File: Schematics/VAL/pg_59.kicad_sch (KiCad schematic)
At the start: 12 parts, among them U6101 F260, U6102 F10, U6103 F260, U6104 F10, U6105 F74, U6106 F74, U6107 F74, U6108 F74, U6109 F37, U6110 F260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

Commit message: Use backplane clocks
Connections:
- net UIR~.SCLK.B2 renamed UIR~.SCLK
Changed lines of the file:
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@@
   (wire (pts (xy 368.3 55.88) (xy 375.92 55.88) ) )
   (wire (pts (xy 368.3 93.98) (xy 375.92 93.98) ) )
-  (global_label "UIR~.SCLK.B2" (shape input) (at 111.76 27.94 180) (fields_autoplaced) (effects (font (size 2.54 2.54) ) (justify right) ) (property "Intersheet References" "${INTERSHEET_REFS}" (id 0) (at 81.7759 27.7813 0) (effects (font (size 2.54 2.54) ) (justify right) ) ) )
+  (global_label "UIR~.SCLK" (shape input) (at 111.76 27.94 180) (fields_autoplaced) (effects (font (size 2.54 2.54) ) (justify right) ) (property "Intersheet References" "${INTERSHEET_REFS}" (id 0) (at 81.7759 27.7813 0) (effects (font (size 2.54 2.54) ) (justify right) ) ) )
   (global_label "WCS.D[0..11]" (shape input) (at 112.6531 38.1 180) (fields_autoplaced) (effects (font (size 2.54 2.54) ) (justify right) ) (property "Intersheet References" "${INTERSHEET_REFS}" (id 0) (at 83.1528 37.9413 0) (effects (font (size 2.54 2.54) ) (justify right) ) ) )
   (bus_entry (at 116.84 40.64) (size 2.54 2.54) )

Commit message: Speed up VAL board
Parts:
- removed U6101, U6103, U6110, U6112: F260, symbol r1000:F260
- removed U6102, U6104: F10, symbol r1000:F10
- removed U6105, U6106, U6107, U6108: F74, symbol r1000:F74
- removed U6109, U6111: F37, symbol r1000:F37
- added U6113, U6115: F521, symbol r1000:F521
- added U6114, U6116: F74, symbol r1000:F74
- added U6117, U6118: F02, symbol r1000:F02
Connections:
- net A_LOOP_DEC: now also U6117.3 (Q)
- net A_LOOP_DEC~: now also U6114.5 (Q), U6117.1 (D0)
- net B_LOOP_DEC: now also U6118.3 (Q)
- net B_LOOP_DEC~: now also U6116.5 (Q), U6118.1 (D0)
- net H2: now also U6117.2 (D1), U6118.2 (D1)
- net PD: now also U6113.1 (E), U6113.12 (B4), U6113.14 (B5), U6113.7 (B2), U6115.1 (E), U6115.12 (B4), U6115.14 (B5), U6115.7 (B2)
- net PU: now also U6113.16 (B6), U6113.18 (B7), U6113.9 (B3), U6114.1 (CL_), U6114.4 (PR_), U6115.16 (B6), U6115.18 (B7), U6115.9 (B3), U6116.1 (CL_), U6116.4 (PR_)
- net UIR~.SCLK: now also U6114.3 (CLK), U6116.3 (CLK)
- net WCS.D0: now also U6113.6 (A2)
- net WCS.D1: now also U6113.8 (A3)
- net WCS.D10: now also U6115.15 (A6)
- net WCS.D11: now also U6115.17 (A7)
- net WCS.D2: now also U6113.11 (A4)
- net WCS.D3: now also U6113.13 (A5)
- net WCS.D4: now also U6113.15 (A6)
- net WCS.D5: now also U6113.17 (A7)
- net WCS.D6: now also U6115.6 (A2)
- net WCS.D7: now also U6115.8 (A3)
- net WCS.D8: now also U6115.11 (A4)
- net WCS.D9: now also U6115.13 (A5)
- new net: U6113.19 (A=B), U6114.2 (D)
- new net: U6115.19 (A=B), U6116.2 (D)
- no-connect marks 0 -> 10
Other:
- note added: "UIR.A0"
- note added: "UIR.A1"
- note added: "UIR.A2"
- note added: "UIR.A3"
- note added: "UIR.A4"
- note added: "UIR.A5"
- note added: "UIR.B0"
- note added: "UIR.B1"
- note added: "UIR.B2"
- note added: "UIR.B3"
- note added: "UIR.B4"
- note added: "UIR.B5"

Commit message: KiCad 6
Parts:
- U6113, U6115: value F521 -> (none)
- U6114, U6116: value F74 -> (none)
- U6117, U6118: value F02 -> (none)

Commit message: Recover from KiCad-6 munging
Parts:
- U6113, U6115: value (none) -> F521
- U6114, U6116: value (none) -> F74
- U6117, U6118: value (none) -> F02

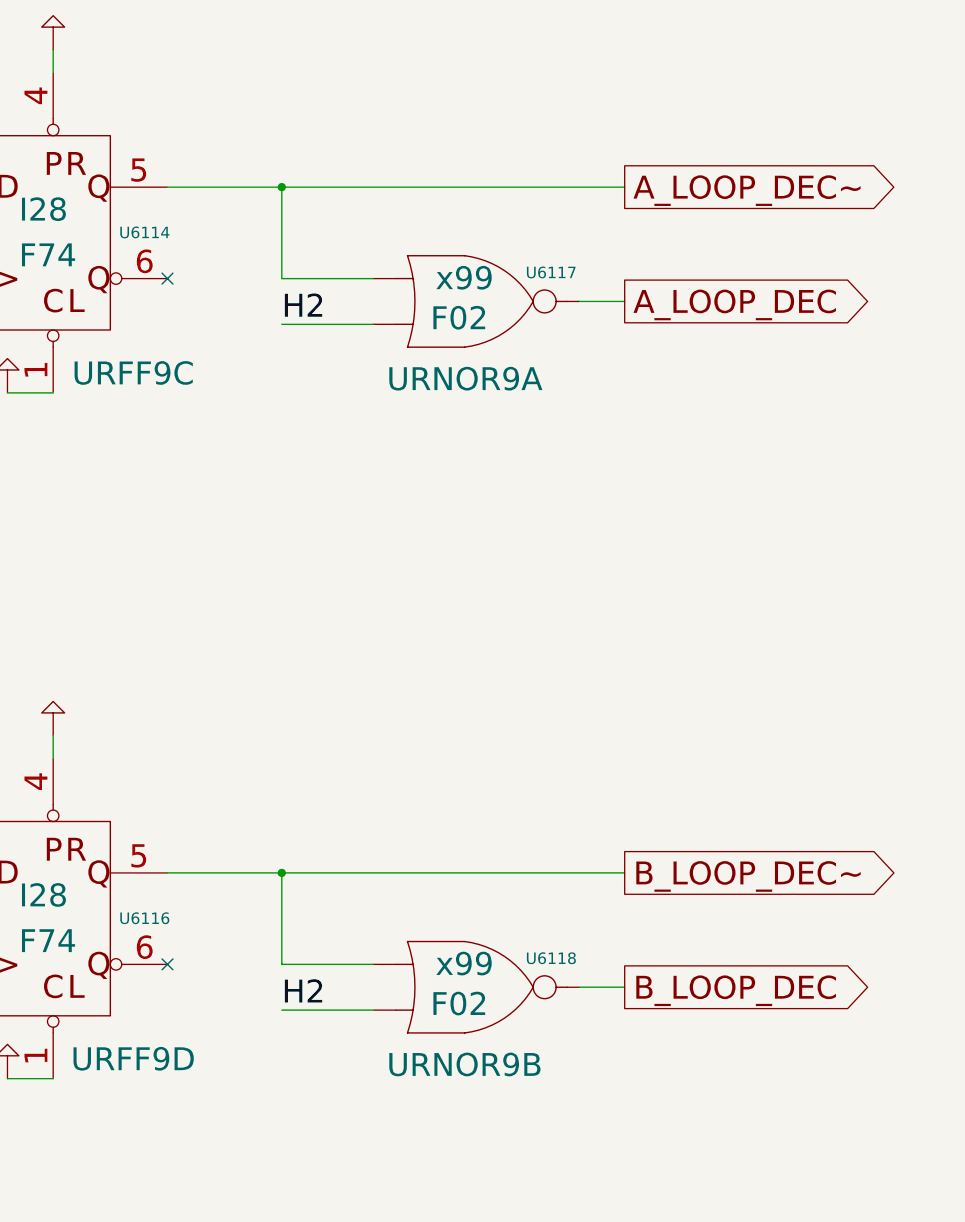
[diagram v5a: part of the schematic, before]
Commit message: Snapshot with some significant speedups.
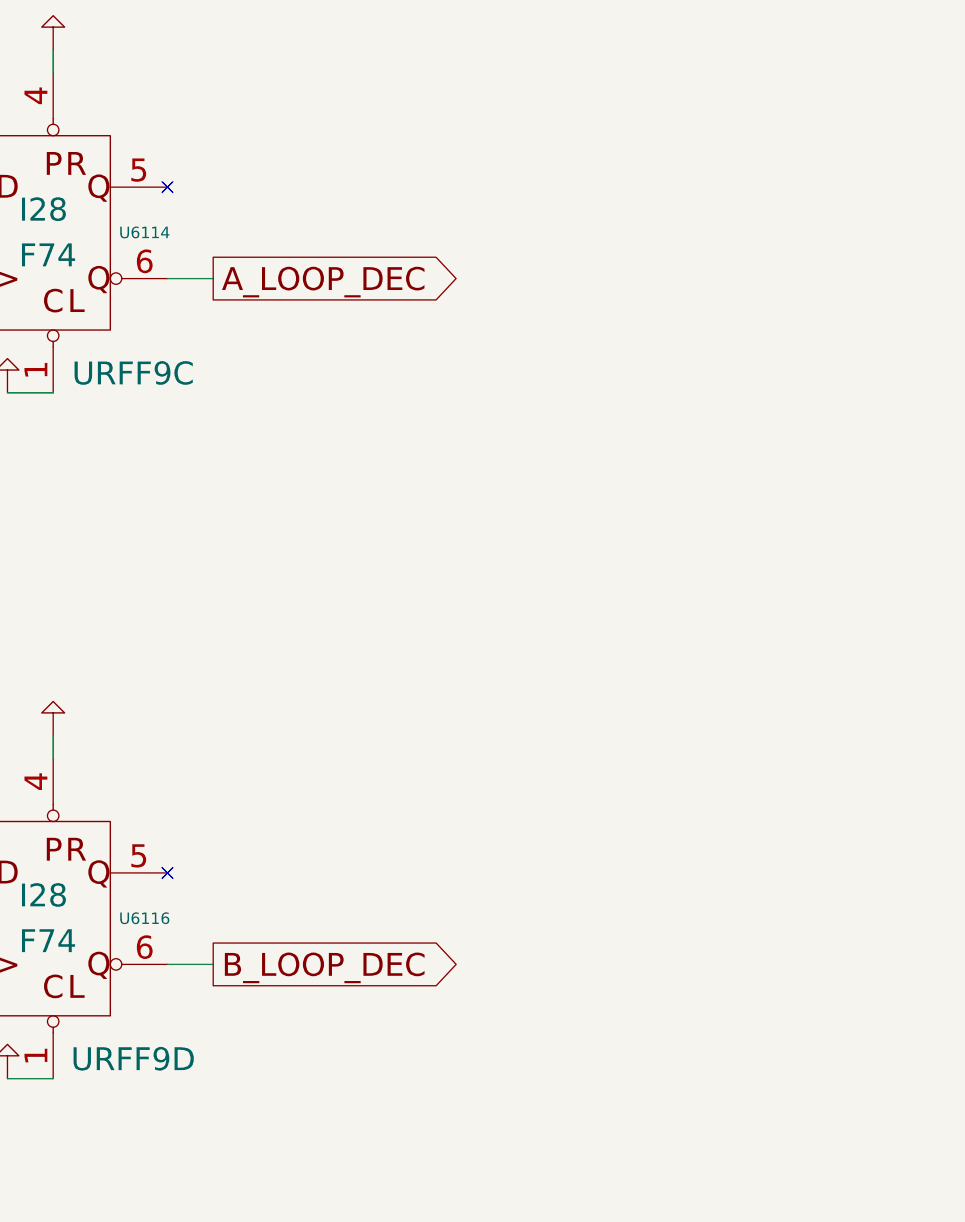
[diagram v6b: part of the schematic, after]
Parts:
- removed U6117, U6118: F02, symbol r1000:F02
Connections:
- net A_LOOP_DEC: now also U6114.6 (Q_)
- net B_LOOP_DEC: now also U6116.6 (Q_)
- net A_LOOP_DEC~: no longer names the net of U6114.5 (Q)
- net B_LOOP_DEC~: no longer names the net of U6116.5 (Q)
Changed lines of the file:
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@@
   (wire (pts (xy 289.56 109.22) (xy 289.56 111.76) ) )
   (wire (pts (xy 289.56 185.42) (xy 289.56 187.96) ) )
-  (wire (pts (xy 302.26 124.46) (xy 314.96 124.46) ) )
-  (wire (pts (xy 302.26 200.66) (xy 314.96 200.66) ) )
-  (wire (pts (xy 314.96 124.46) (xy 353.06 124.46) ) )
-  (wire (pts (xy 314.96 134.62) (xy 314.96 124.46) ) )
-  (wire (pts (xy 314.96 139.7) (xy 325.12 139.7) ) )
-  (wire (pts (xy 314.96 200.66) (xy 353.06 200.66) ) )
-  (wire (pts (xy 314.96 210.82) (xy 314.96 200.66) ) )
-  (wire (pts (xy 314.96 215.9) (xy 325.12 215.9) ) )
-  (wire (pts (xy 325.12 134.62) (xy 314.96 134.62) ) )
-  (wire (pts (xy 325.12 210.82) (xy 314.96 210.82) ) )
-  (wire (pts (xy 347.98 137.16) (xy 353.06 137.16) ) )
-  (wire (pts (xy 347.98 213.36) (xy 353.06 213.36) ) )
+  (wire (pts (xy 302.26 134.62) (xy 307.34 134.62) ) )
+  (wire (pts (xy 302.26 210.82) (xy 307.34 210.82) ) )
   (wire (pts (xy 76.2 12.7) (xy 88.9 12.7) ) )
   (wire (pts (xy 76.2 22.86) (xy 88.9 22.86) ) )
@@
   (symbol (lib_id "r1000:PU") (at 289.56 109.22 0) (unit 1) (in_bom yes) (on_board yes) (property "Reference" "#PWR06117" (id 0) (at 289.56 109.22 0) (effects (font (size 1.27 1.27) ) hide ) ) (property "Value" "PU" (id 1) (at 289.56 109.22 0) (effects (font (size 1.27 1.27) ) hide ) ) (property "Footprint" "" (id 2) (at 289.56 109.22 0) (effects (font (size 1.27 1.27) ) hide ) ) (property "Datasheet" "" (id 3) (at 289.56 109.22 0) (effects (font (size 1.27 1.27) ) hide ) ) (pin "1") )
   (symbol (lib_id "r1000:PU") (at 289.56 185.42 0) (unit 1) (in_bom yes) (on_board yes) (property "Reference" "#PWR06122" (id 0) (at 289.56 185.42 0) (effects (font (size 1.27 1.27) ) hide ) ) (property "Value" "PU" (id 1) (at 289.56 185.42 0) (effects (font (size 1.27 1.27) ) hide ) ) (property "Footprint" "" (id 2) (at 289.56 185.42 0) (effects (font (size 1.27 1.27) ) hide ) ) (property "Datasheet" "" (id 3) (at 289.56 185.42 0) (effects (font (size 1.27 1.27) ) hide ) ) (pin "1") )
-  (no_connect (at 302.26 134.62) )
-  (no_connect (at 302.26 210.82) )
-  (junction (at 314.96 124.46) (diameter 0) (color 0 0 0 0) )
-  (label "H2" (at 314.96 139.7 0) (effects (font (size 2.54 2.54) ) (justify left bottom) ) )
-  (junction (at 314.96 200.66) (diameter 0) (color 0 0 0 0) )
-  (label "H2" (at 314.96 215.9 0) (effects (font (size 2.54 2.54) ) (justify left bottom) ) )
-  (symbol (lib_id "r1000:F02") (at 332.74 134.62 0) (unit 1) (in_bom yes) (on_board yes) (property "Reference" "U6117" (id 0) (at 344.9 133.985 0) (effects (font (size 1.27 1.27) ) ) ) (property "Value" "F02" (id 1) (at 331.47 139.065 0) (effects (font (size 2.54 2.54) ) (justify left) ) ) (property "Footprint" "" (id 2) (at 332.74 134.62 0) (effects (font (size 1.27 1.27) ) hide ) ) (property "Datasheet" "" (id 3) (at 332.74 134.62 0) (effects (font (size 1.27 1.27) ) hide ) ) (property "Location" "x99" (id 4) (at 335.28 134.62 0) (effects (font (size 2.54 2.54) ) ) ) (property "Name" "URNOR9A" (id 5) (at 335.28 147.32 0) (effects (font (size 2.54 2.54) ) (justify bottom) ) ) (pin "1") (pin "2") (pin "3") )
-  (symbol (lib_id "r1000:F02") (at 332.74 210.82 0) (unit 1) (in_bom yes) (on_board yes) (property "Reference" "U6118" (id 0) (at 344.9 210.185 0) (effects (font (size 1.27 1.27) ) ) ) (property "Value" "F02" (id 1) (at 331.47 215.265 0) (effects (font (size 2.54 2.54) ) (justify left) ) ) (property "Footprint" "" (id 2) (at 332.74 210.82 0) (effects (font (size 1.27 1.27) ) hide ) ) (property "Datasheet" "" (id 3) (at 332.74 210.82 0) (effects (font (size 1.27 1.27) ) hide ) ) (property "Location" "x99" (id 4) (at 335.28 210.82 0) (effects (font (size 2.54 2.54) ) ) ) (property "Name" "URNOR9B" (id 5) (at 335.28 223.52 0) (effects (font (size 2.54 2.54) ) (justify bottom) ) ) (pin "1") (pin "2") (pin "3") )
-  (global_label "A_LOOP_DEC~" (shape output) (at 353.06 124.46 0) (fields_autoplaced) (effects (font (size 2.54 2.54) ) (justify left) ) (property "Intersheet References" "${INTERSHEET_REFS}" (id 0) (at 383.0441 124.3013 0) (effects (font (size 1.905 1.905) ) (justify left) ) ) )
-  (global_label "A_LOOP_DEC" (shape output) (at 353.06 137.16 0) (fields_autoplaced) (effects (font (size 2.54 2.54) ) (justify left) ) (property "Intersheet References" "${INTERSHEET_REFS}" (id 0) (at 381.2298 137.0013 0) (effects (font (size 1.905 1.905) ) (justify left) ) ) )
-  (global_label "B_LOOP_DEC~" (shape output) (at 353.06 200.66 0) (fields_autoplaced) (effects (font (size 2.54 2.54) ) (justify left) ) (property "Intersheet References" "${INTERSHEET_REFS}" (id 0) (at 383.407 200.5013 0) (effects (font (size 1.905 1.905) ) (justify left) ) ) )
-  (global_label "B_LOOP_DEC" (shape output) (at 353.06 213.36 0) (fields_autoplaced) (effects (font (size 2.54 2.54) ) (justify left) ) (property "Intersheet References" "${INTERSHEET_REFS}" (id 0) (at 381.5927 213.2013 0) (effects (font (size 1.905 1.905) ) (justify left) ) ) )
+  (no_connect (at 302.26 124.46) )
+  (no_connect (at 302.26 200.66) )
+  (global_label "A_LOOP_DEC" (shape output) (at 307.34 134.62 0) (fields_autoplaced) (effects (font (size 2.54 2.54) ) (justify left) ) (property "Intersheet References" "${INTERSHEET_REFS}" (id 0) (at 335.5098 134.4613 0) (effects (font (size 1.905 1.905) ) (justify left) ) ) )
+  (global_label "B_LOOP_DEC" (shape output) (at 307.34 210.82 0) (fields_autoplaced) (effects (font (size 2.54 2.54) ) (justify left) ) (property "Intersheet References" "${INTERSHEET_REFS}" (id 0) (at 335.8727 210.6613 0) (effects (font (size 1.905 1.905) ) (justify left) ) ) )
 )

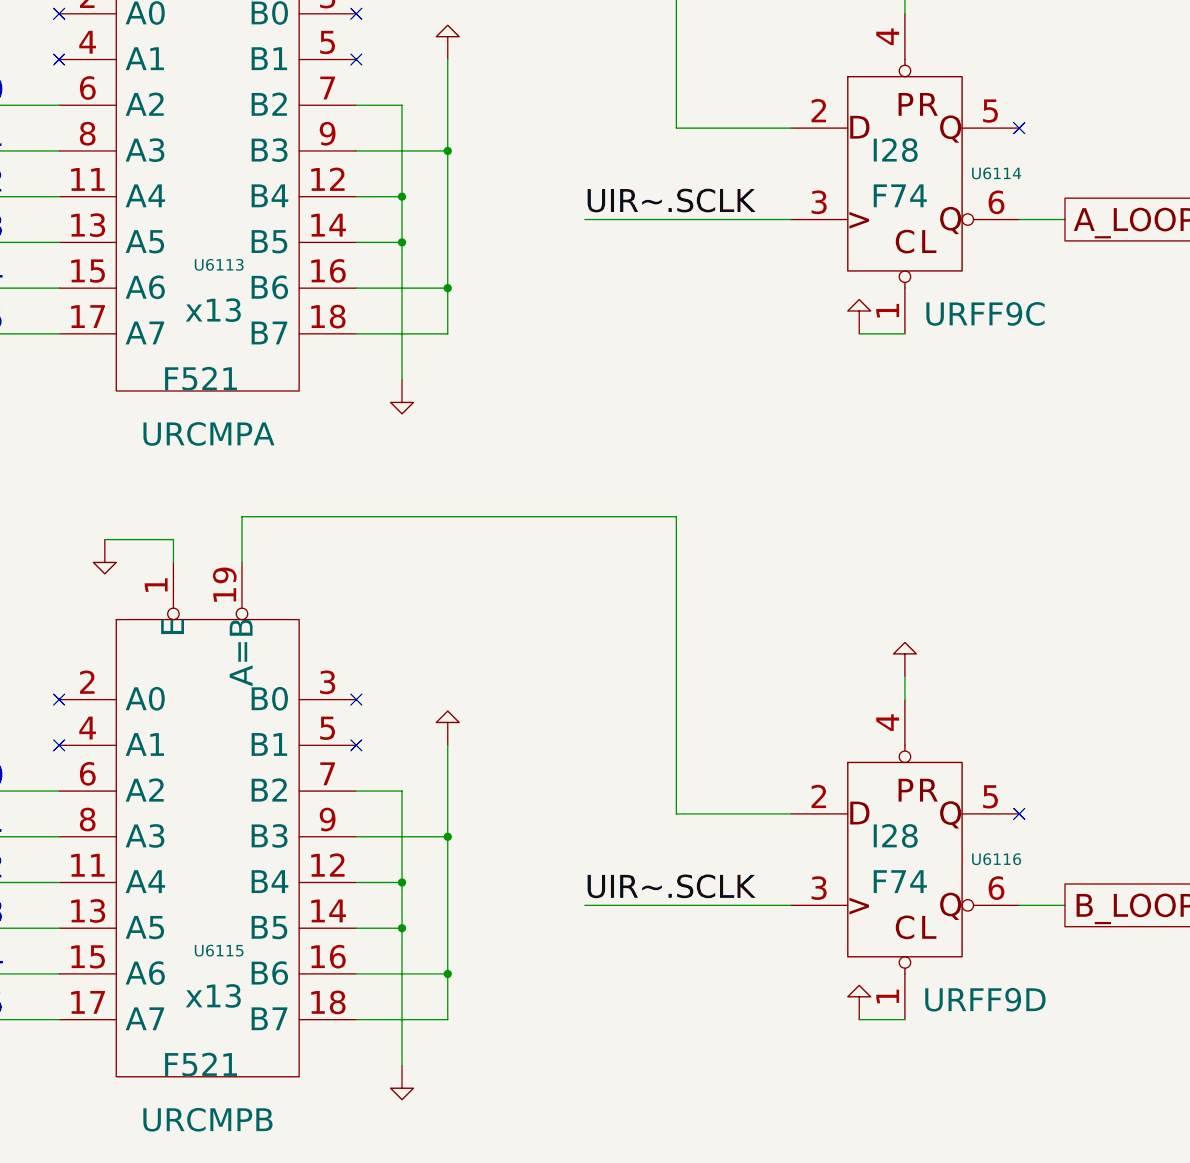
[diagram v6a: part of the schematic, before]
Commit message: Revert page 44 to older working (P2FP) version
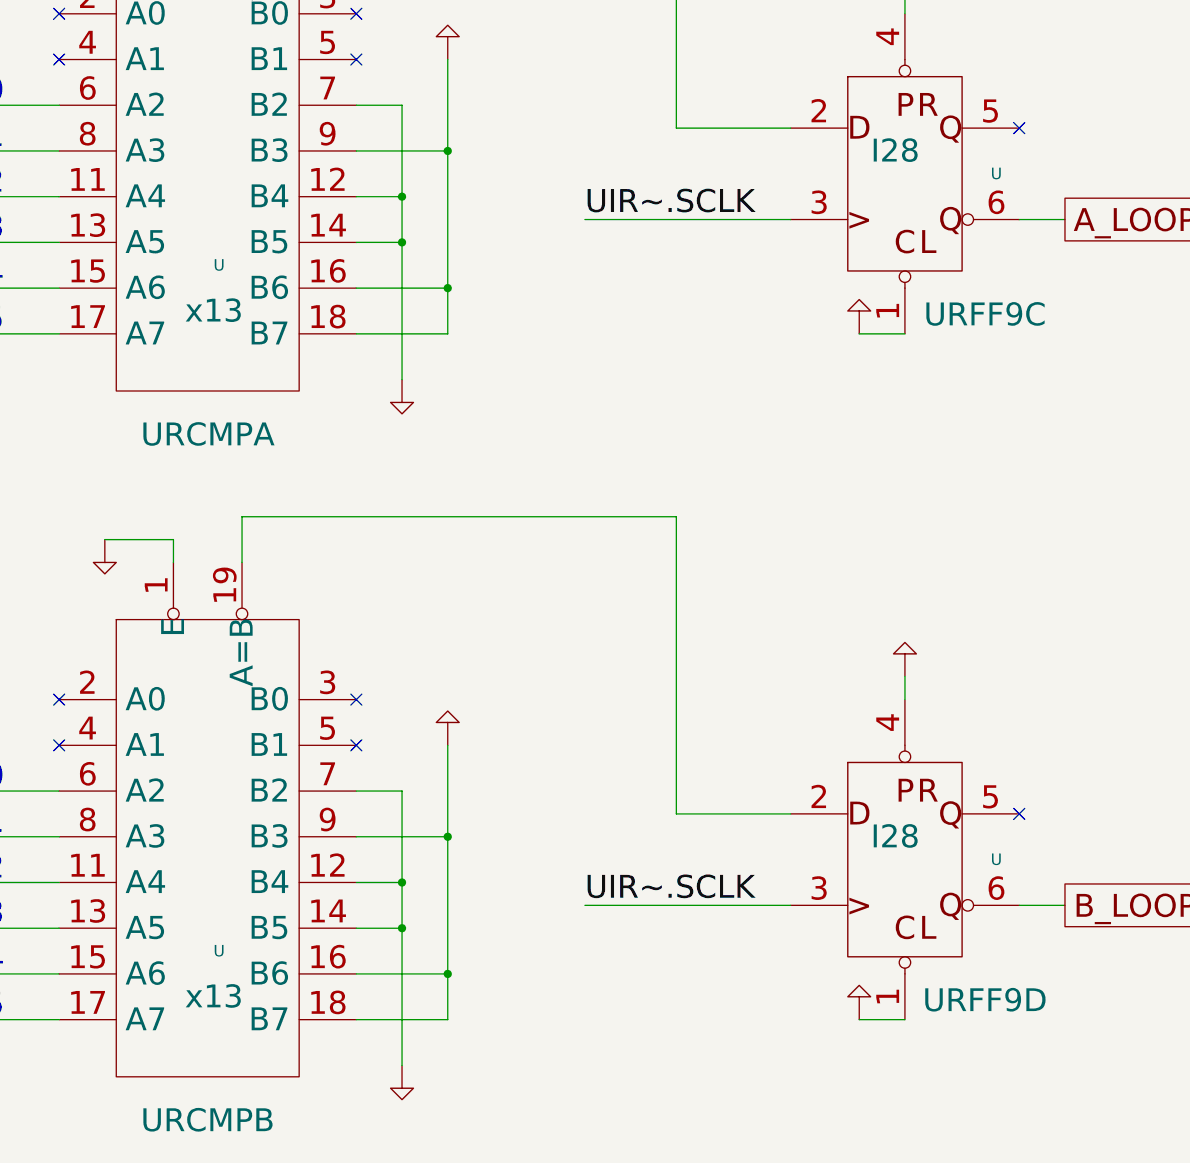
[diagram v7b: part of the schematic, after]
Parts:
- removed U6113, U6115: F521, symbol r1000:F521
- removed U6114, U6116: F74, symbol r1000:F74
- added U (x2): (no value), symbol r1000:F74
- added U (x2): (no value), symbol r1000:F521
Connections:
- net A_LOOP_DEC: now also U.6 (Q_)
- net B_LOOP_DEC: now also U.6 (Q_)
- net PD: now also U.1 (E), U.1 (E), U.12 (B4), U.12 (B4), U.14 (B5), U.14 (B5), U.7 (B2), U.7 (B2)
- net PU: now also U.1 (CL_), U.1 (CL_), U.16 (B6), U.16 (B6), U.18 (B7), U.18 (B7), U.4 (PR_), U.4 (PR_), U.9 (B3), U.9 (B3)
- net UIR~.SCLK: now also U.3 (CLK), U.3 (CLK)
- net WCS.D0: now also U.6 (A2)
- net WCS.D1: now also U.8 (A3)
- net WCS.D10: now also U.15 (A6)
- net WCS.D11: now also U.17 (A7)
- net WCS.D2: now also U.11 (A4)
- net WCS.D3: now also U.13 (A5)
- net WCS.D4: now also U.15 (A6)
- net WCS.D5: now also U.17 (A7)
- net WCS.D6: now also U.6 (A2)
- net WCS.D7: now also U.8 (A3)
- net WCS.D8: now also U.11 (A4)
- net WCS.D9: now also U.13 (A5)
- new net: U.19 (A=B), U.2 (D) (x2)
